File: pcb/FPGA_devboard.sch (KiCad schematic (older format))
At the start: 2 parts, among them X3 AC7020, X4 Conn_02x05_Odd_Even

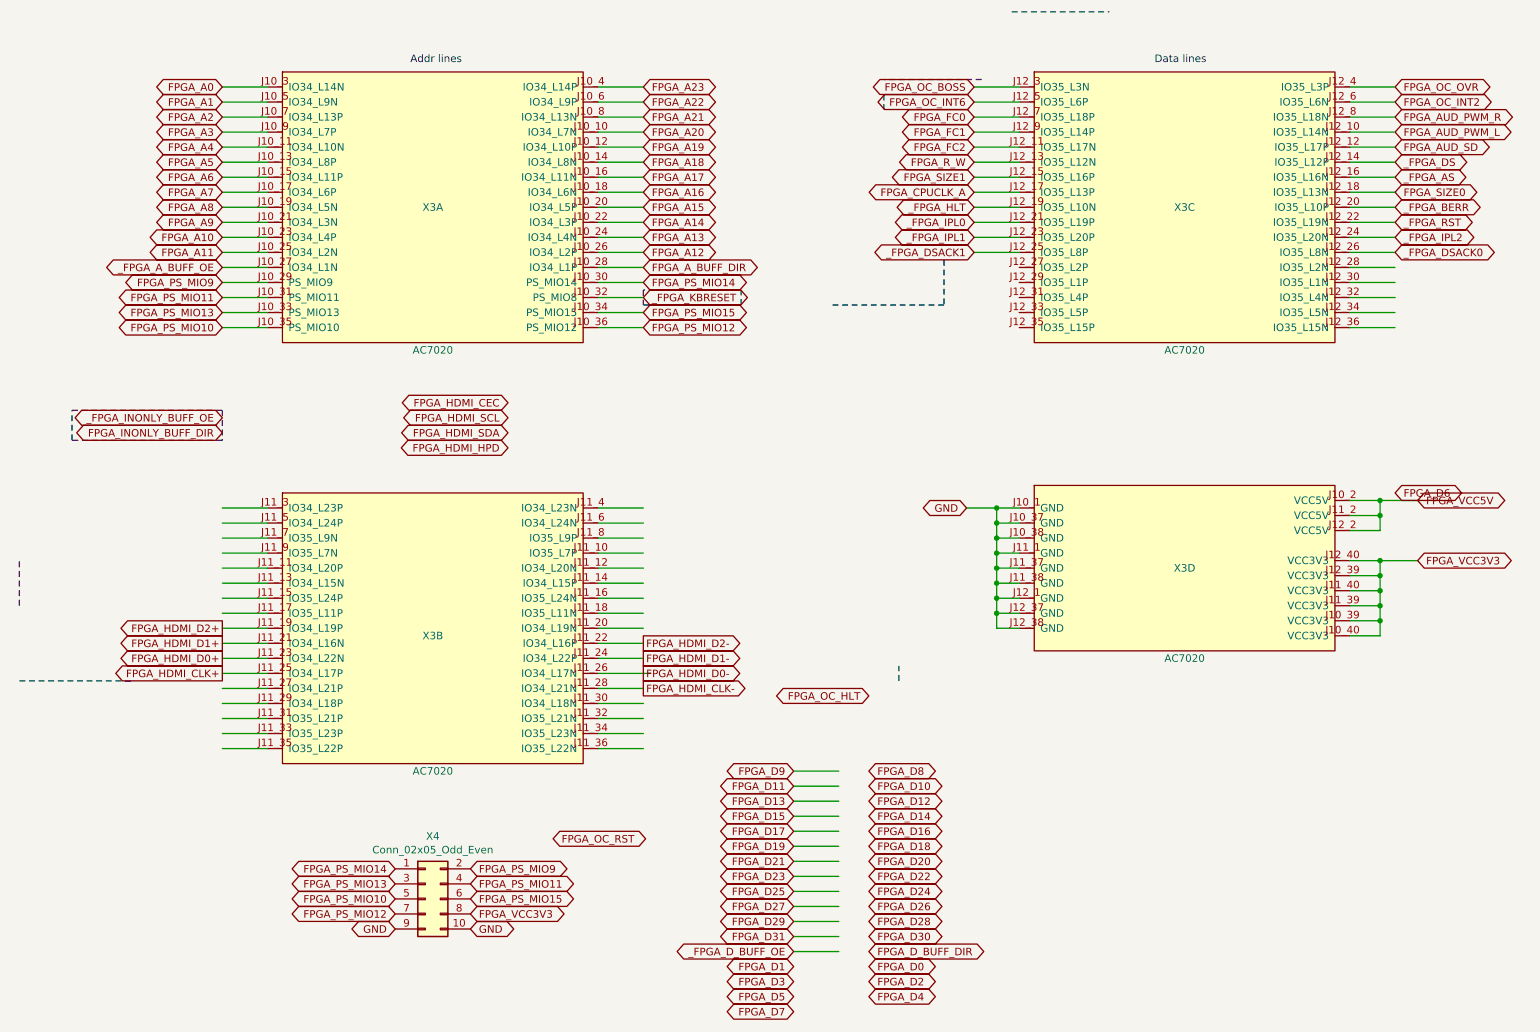
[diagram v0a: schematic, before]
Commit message: wire length aligns
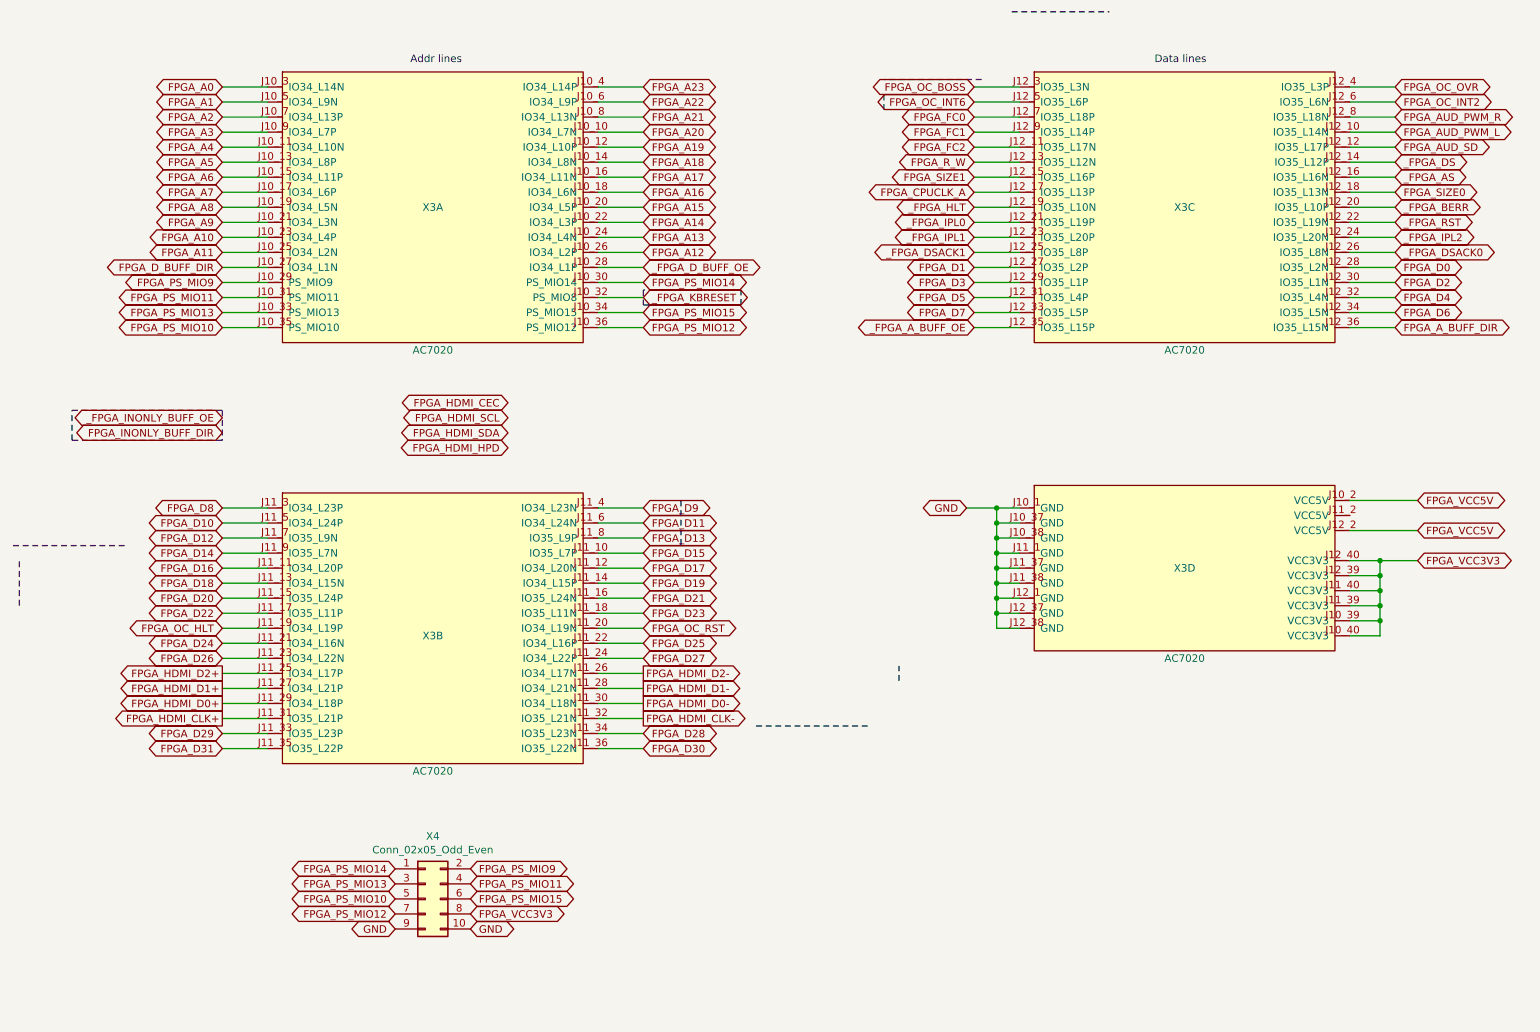
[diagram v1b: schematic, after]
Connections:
- wire segments 146 -> 134
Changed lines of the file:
@@
 	4300 6000 4600 6000
 Wire Wire Line
-	5600 7350 5900 7350
-Wire Wire Line
 	6800 1800 7100 1800
 Wire Wire Line
@@
 	6800 2100 7100 2100
 Wire Wire Line
-	5600 6150 5900 6150
-Wire Wire Line
-	5600 6250 5900 6250
-Wire Wire Line
-	5600 6350 5900 6350
-Wire Wire Line
-	5600 6450 5900 6450
-Wire Wire Line
-	5600 6550 5900 6550
-Wire Wire Line
-	5600 6650 5900 6650
-Wire Wire Line
-	5600 6750 5900 6750
-Wire Wire Line
-	5600 6850 5900 6850
-Wire Wire Line
-	5600 6950 5900 6950
-Wire Wire Line
-	5600 7050 5900 7050
-Wire Wire Line
-	5600 7150 5900 7150
-Wire Wire Line
-	5600 7250 5900 7250
+	6800 2800 7100 2800
+Wire Wire Line
+	6800 2900 7100 2900
+Wire Wire Line
+	6800 3000 7100 3000
+Wire Wire Line
+	6800 3100 7100 3100
+Wire Wire Line
+	6800 3200 7100 3200
 Wire Wire Line
 	9300 1600 9600 1600
@@
 Wire Wire Line
 	7100 5100 6950 5100
-Wire Wire Line
-	9300 4350 9500 4350
-Wire Wire Line
-	9300 4550 9500 4550
 Wire Wire Line
 	9300 4750 9500 4750
@@
 Text GLabel 9750 4350 2    50   BiDi ~ 0
 FPGA_VCC5V
-Wire Wire Line
-	9500 4350 9500 4450
-Connection ~ 9500 4350
-Wire Wire Line
-	9500 4350 9750 4350
-Connection ~ 9500 4450
-Wire Wire Line
-	9500 4450 9300 4450
-Wire Wire Line
-	9500 4450 9500 4550
 Wire Wire Line
 	9500 4750 9500 4850
@@
 Text GLabel 4600 1600 2    50   BiDi ~ 0
 FPGA_A23
+Text GLabel 9600 3200 2    50   BiDi ~ 0
+FPGA_A_BUFF_DIR
+Text GLabel 6800 3200 0    50   BiDi ~ 0
+_FPGA_A_BUFF_OE
+Text GLabel 9600 2800 2    50   BiDi ~ 0
+FPGA_D0
+Text GLabel 6800 2800 0    50   BiDi ~ 0
+FPGA_D1
+Text GLabel 9600 2900 2    50   BiDi ~ 0
+FPGA_D2
+Text GLabel 6800 2900 0    50   BiDi ~ 0
+FPGA_D3
+Text GLabel 9600 3000 2    50   BiDi ~ 0
+FPGA_D4
+Text GLabel 6800 3000 0    50   BiDi ~ 0
+FPGA_D5
+Text GLabel 9600 3100 2    50   BiDi ~ 0
+FPGA_D6
+Text GLabel 6800 3100 0    50   BiDi ~ 0
+FPGA_D7
+Text GLabel 1800 4400 0    50   BiDi ~ 0
+FPGA_D8
+Text GLabel 4600 4400 2    50   BiDi ~ 0
+FPGA_D9
+Text GLabel 1800 4500 0    50   BiDi ~ 0
+FPGA_D10
+Text GLabel 4600 4500 2    50   BiDi ~ 0
+FPGA_D11
+Text GLabel 1800 4600 0    50   BiDi ~ 0
+FPGA_D12
+Text GLabel 4600 4600 2    50   BiDi ~ 0
+FPGA_D13
+Text GLabel 1800 4700 0    50   BiDi ~ 0
+FPGA_D14
+Text GLabel 4600 4700 2    50   BiDi ~ 0
+FPGA_D15
+Text GLabel 1800 4800 0    50   BiDi ~ 0
+FPGA_D16
+Text GLabel 4600 4800 2    50   BiDi ~ 0
+FPGA_D17
+Text GLabel 1800 4900 0    50   BiDi ~ 0
+FPGA_D18
+Text GLabel 4600 4900 2    50   BiDi ~ 0
+FPGA_D19
+Text GLabel 1800 5000 0    50   BiDi ~ 0
+FPGA_D20
+Text GLabel 4600 5000 2    50   BiDi ~ 0
+FPGA_D21
+Text GLabel 1800 5100 0    50   BiDi ~ 0
+FPGA_D22
+Text GLabel 4600 5100 2    50   BiDi ~ 0
+FPGA_D23
+Text GLabel 1800 5300 0    50   BiDi ~ 0
+FPGA_D24
+Text GLabel 4600 5300 2    50   BiDi ~ 0
+FPGA_D25
+Text GLabel 1800 5400 0    50   BiDi ~ 0
+FPGA_D26
+Text GLabel 4600 5400 2    50   BiDi ~ 0
+FPGA_D27
+Text GLabel 4600 5900 2    50   BiDi ~ 0
+FPGA_D28
+Text GLabel 1800 5900 0    50   BiDi ~ 0
+FPGA_D29
+Text GLabel 4600 6000 2    50   BiDi ~ 0
+FPGA_D30
+Text GLabel 1800 6000 0    50   BiDi ~ 0
+FPGA_D31
+Text GLabel 1800 2800 0    50   BiDi ~ 0
+FPGA_D_BUFF_DIR
 Text GLabel 4600 2800 2    50   BiDi ~ 0
-FPGA_A_BUFF_DIR
-Text GLabel 1800 2800 0    50   BiDi ~ 0
-_FPGA_A_BUFF_OE
-Text GLabel 6100 7450 2    50   BiDi ~ 0
-FPGA_D0
-Text GLabel 5600 7450 0    50   BiDi ~ 0
-FPGA_D1
-Text GLabel 6100 7550 2    50   BiDi ~ 0
-FPGA_D2
-Text GLabel 5600 7550 0    50   BiDi ~ 0
-FPGA_D3
-Text GLabel 6100 7650 2    50   BiDi ~ 0
-FPGA_D4
-Text GLabel 5600 7650 0    50   BiDi ~ 0
-FPGA_D5
-Text GLabel 9600 4300 2    50   BiDi ~ 0
-FPGA_D6
-Text GLabel 5600 7750 0    50   BiDi ~ 0
-FPGA_D7
-Text GLabel 6100 6150 2    50   BiDi ~ 0
-FPGA_D8
-Text GLabel 5600 6150 0    50   BiDi ~ 0
-FPGA_D9
-Text GLabel 6100 6250 2    50   BiDi ~ 0
-FPGA_D10
-Text GLabel 5600 6250 0    50   BiDi ~ 0
-FPGA_D11
-Text GLabel 6100 6350 2    50   BiDi ~ 0
-FPGA_D12
-Text GLabel 5600 6350 0    50   BiDi ~ 0
-FPGA_D13
-Text GLabel 6100 6450 2    50   BiDi ~ 0
-FPGA_D14
-Text GLabel 5600 6450 0    50   BiDi ~ 0
-FPGA_D15
-Text GLabel 6100 6550 2    50   BiDi ~ 0
-FPGA_D16
-Text GLabel 5600 6550 0    50   BiDi ~ 0
-FPGA_D17
-Text GLabel 6100 6650 2    50   BiDi ~ 0
-FPGA_D18
-Text GLabel 5600 6650 0    50   BiDi ~ 0
-FPGA_D19
-Text GLabel 6100 6750 2    50   BiDi ~ 0
-FPGA_D20
-Text GLabel 5600 6750 0    50   BiDi ~ 0
-FPGA_D21
-Text GLabel 6100 6850 2    50   BiDi ~ 0
-FPGA_D22
-Text GLabel 5600 6850 0    50   BiDi ~ 0
-FPGA_D23
-Text GLabel 6100 6950 2    50   BiDi ~ 0
-FPGA_D24
-Text GLabel 5600 6950 0    50   BiDi ~ 0
-FPGA_D25
-Text GLabel 6100 7050 2    50   BiDi ~ 0
-FPGA_D26
-Text GLabel 5600 7050 0    50   BiDi ~ 0
-FPGA_D27
-Text GLabel 6100 7150 2    50   BiDi ~ 0
-FPGA_D28
-Text GLabel 5600 7150 0    50   BiDi ~ 0
-FPGA_D29
-Text GLabel 6100 7250 2    50   BiDi ~ 0
-FPGA_D30
-Text GLabel 5600 7250 0    50   BiDi ~ 0
-FPGA_D31
-Text GLabel 6100 7350 2    50   BiDi ~ 0
-FPGA_D_BUFF_DIR
-Text GLabel 5600 7350 0    50   BiDi ~ 0
 _FPGA_D_BUFF_OE
-Text GLabel 9600 1900 2    50   BiDi ~ 0
-FPGA_AUD_PWM_L
-Text GLabel 9600 1800 2    50   BiDi ~ 0
-FPGA_AUD_PWM_R
-Text GLabel 9600 2000 2    50   BiDi ~ 0
-FPGA_AUD_SD
-Text GLabel 4000 6600 2    50   BiDi ~ 0
+Text GLabel 4600 5200 2    50   BiDi ~ 0
 FPGA_OC_RST
 Text GLabel 2950 7200 0    50   BiDi ~ 0
@@
 	450  5050 450  4750
 Wire Notes Line
-	450  5550 1200 5550
-Wire Notes Line
-	6600 3050 5850 3050
+	5350 5850 6100 5850
+Wire Notes Line
+	1150 4650 400  4650
 Wire Notes Line
 	6200 1650 6200 1750
@@
 Wire Notes Line
 	4600 3050 5250 3050
-Text GLabel 1800 5200 0    50   Output ~ 0
+Text GLabel 1800 5500 0    50   Output ~ 0
 FPGA_HDMI_D2+
-Text GLabel 4600 5300 2    50   Output ~ 0
+Text GLabel 4600 5500 2    50   Output ~ 0
 FPGA_HDMI_D2-
-Text GLabel 1800 5300 0    50   Output ~ 0
+Text GLabel 1800 5600 0    50   Output ~ 0
 FPGA_HDMI_D1+
-Text GLabel 1800 5400 0    50   Output ~ 0
+Text GLabel 1800 5700 0    50   Output ~ 0
 FPGA_HDMI_D0+
-Text GLabel 4600 5500 2    50   Output ~ 0
+Text GLabel 4600 5700 2    50   Output ~ 0
 FPGA_HDMI_D0-
-Text GLabel 4600 5400 2    50   Output ~ 0
+Text GLabel 4600 5600 2    50   Output ~ 0
 FPGA_HDMI_D1-
-Text GLabel 1800 5500 0    50   Output ~ 0
+Text GLabel 1800 5800 0    50   Output ~ 0
 FPGA_HDMI_CLK+
 Wire Notes Line
@@
 Wire Notes Line
 	800  3750 1800 3750
-Text GLabel 9600 2200 2    50   BiDi ~ 0
-_FPGA_AS
-Text GLabel 6800 2200 0    50   BiDi ~ 0
-FPGA_SIZE1
-Text GLabel 9600 2300 2    50   BiDi ~ 0
-FPGA_SIZE0
 Text GLabel 1800 3900 0    50   BiDi ~ 0
 FPGA_INONLY_BUFF_DIR
@@
 _FPGA_INONLY_BUFF_OE
 Wire Notes Line
-	6600 2750 6600 3050
-Text GLabel 4600 5600 2    50   Output ~ 0
+	4850 4350 4850 4650
+Text GLabel 4600 5800 2    50   Output ~ 0
 FPGA_HDMI_CLK-
 Wire Wire Line
@@
 FPGA_HDMI_HPD
 Wire Wire Line
-	4300 5500 4650 5500
+	4300 5500 4600 5500
 Text GLabel 3450 6800 2    50   BiDi ~ 0
 FPGA_PS_MIO9
@@
 Wire Notes Line
 	6850 1550 6200 1550
-Text GLabel 6800 2600 0    50   BiDi ~ 0
-_FPGA_IPL1
-Text GLabel 6800 2500 0    50   BiDi ~ 0
-_FPGA_IPL0
-Text GLabel 6800 2400 0    50   BiDi ~ 0
-_FPGA_HLT
-Text GLabel 6800 2700 0    50   BiDi ~ 0
-_FPGA_DSACK1
 Text GLabel 9600 1600 2    50   BiDi ~ 0
 FPGA_OC_OVR
 Text GLabel 6800 1700 0    50   BiDi ~ 0
 FPGA_OC_INT6
-Text GLabel 6100 5650 0    50   BiDi ~ 0
+Text GLabel 1800 5200 0    50   BiDi ~ 0
 FPGA_OC_HLT
 Text GLabel 6800 1600 0    50   BiDi ~ 0
 FPGA_OC_BOSS
+Wire Wire Line
+	6800 2200 7100 2200
+Wire Wire Line
+	7100 2300 6800 2300
+Wire Wire Line
+	6800 2400 7100 2400
+Wire Wire Line
+	7100 2500 6800 2500
+Wire Wire Line
+	6800 2600 7100 2600
+Wire Wire Line
+	7100 1600 6800 1600
+Wire Wire Line
+	6800 1700 7100 1700
+Wire Wire Line
+	7100 2700 6800 2700
+Text GLabel 9750 4550 2    50   BiDi ~ 0
+FPGA_VCC5V
+Wire Wire Line
+	9300 4350 9750 4350
+Wire Wire Line
+	9300 4550 9750 4550
+Text GLabel 9600 2100 2    50   BiDi ~ 0
+_FPGA_DS
+Text GLabel 9600 2300 2    50   BiDi ~ 0
+FPGA_SIZE0
+Text GLabel 9600 2200 2    50   BiDi ~ 0
+_FPGA_AS
+Text GLabel 9600 2000 2    50   BiDi ~ 0
+FPGA_AUD_SD
+Text GLabel 9600 1800 2    50   BiDi ~ 0
+FPGA_AUD_PWM_R
+Text GLabel 9600 1900 2    50   BiDi ~ 0
+FPGA_AUD_PWM_L
+Text GLabel 6800 2000 0    50   BiDi ~ 0
+FPGA_FC2
+Text GLabel 6800 1900 0    50   BiDi ~ 0
+FPGA_FC1
+Text GLabel 6800 1800 0    50   BiDi ~ 0
+FPGA_FC0
 Text GLabel 6800 2100 0    50   BiDi ~ 0
 FPGA_R_W
-Text GLabel 6800 1800 0    50   BiDi ~ 0
-FPGA_FC0
-Text GLabel 6800 1900 0    50   BiDi ~ 0
-FPGA_FC1
-Text GLabel 6800 2000 0    50   BiDi ~ 0
-FPGA_FC2
-Text GLabel 9600 2100 2    50   BiDi ~ 0
-_FPGA_DS
-Wire Wire Line
-	6800 2200 7100 2200
-Wire Wire Line
-	7100 2300 6800 2300
-Wire Wire Line
-	6800 2400 7100 2400
-Wire Wire Line
-	7100 2500 6800 2500
-Wire Wire Line
-	6800 2600 7100 2600
-Wire Wire Line
-	7100 1600 6800 1600
-Wire Wire Line
-	6800 1700 7100 1700
-Wire Wire Line
-	7100 2700 6800 2700
+Text GLabel 6800 2200 0    50   BiDi ~ 0
+FPGA_SIZE1
+Text GLabel 6800 2300 0    50   BiDi ~ 0
+FPGA_CPUCLK_A
+Text GLabel 6800 2700 0    50   BiDi ~ 0
+_FPGA_DSACK1
+Text GLabel 6800 2400 0    50   BiDi ~ 0
+_FPGA_HLT
+Text GLabel 6800 2500 0    50   BiDi ~ 0
+_FPGA_IPL0
+Text GLabel 6800 2600 0    50   BiDi ~ 0
+_FPGA_IPL1
+Text GLabel 9600 2400 2    50   BiDi ~ 0
+_FPGA_BERR
+Text GLabel 9600 2500 2    50   BiDi ~ 0
+_FPGA_RST
+Text GLabel 9600 2600 2    50   BiDi ~ 0
+_FPGA_IPL2
 Text GLabel 9600 2700 2    50   BiDi ~ 0
 _FPGA_DSACK0
-Text GLabel 9600 2600 2    50   BiDi ~ 0
-_FPGA_IPL2
-Text GLabel 9600 2500 2    50   BiDi ~ 0
-_FPGA_RST
-Text GLabel 9600 2400 2    50   BiDi ~ 0
-_FPGA_BERR
-Text GLabel 6800 2300 0    50   BiDi ~ 0
-FPGA_CPUCLK_A
 $EndSCHEMATC

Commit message: Some more work done
I'm too lazy to think about commit messages in my pet project, really
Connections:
- net FPGA_VCC5V renamed FPGA_VCC5V_1
- net FPGA_VCC5V_1: no longer X3.J12_2 (VCC5V)
- new net FPGA_VCC5V_2: X3.J12_2 (VCC5V)
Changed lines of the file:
@@
 	6950 5200 7100 5200
 Text GLabel 9750 4350 2    50   BiDi ~ 0
-FPGA_VCC5V
+FPGA_VCC5V_1
 Wire Wire Line
 	9500 4750 9500 4850
@@
 	7100 2700 6800 2700
 Text GLabel 9750 4550 2    50   BiDi ~ 0
-FPGA_VCC5V
+FPGA_VCC5V_2
 Wire Wire Line
 	9300 4350 9750 4350

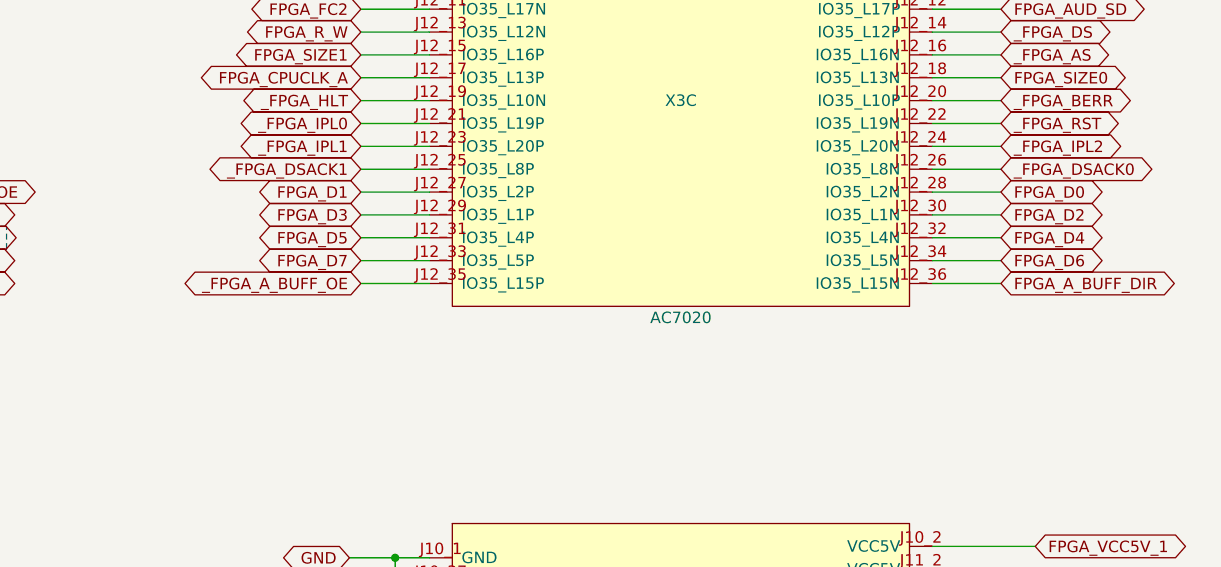
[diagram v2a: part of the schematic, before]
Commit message: bigger vias, fixing DRC issues
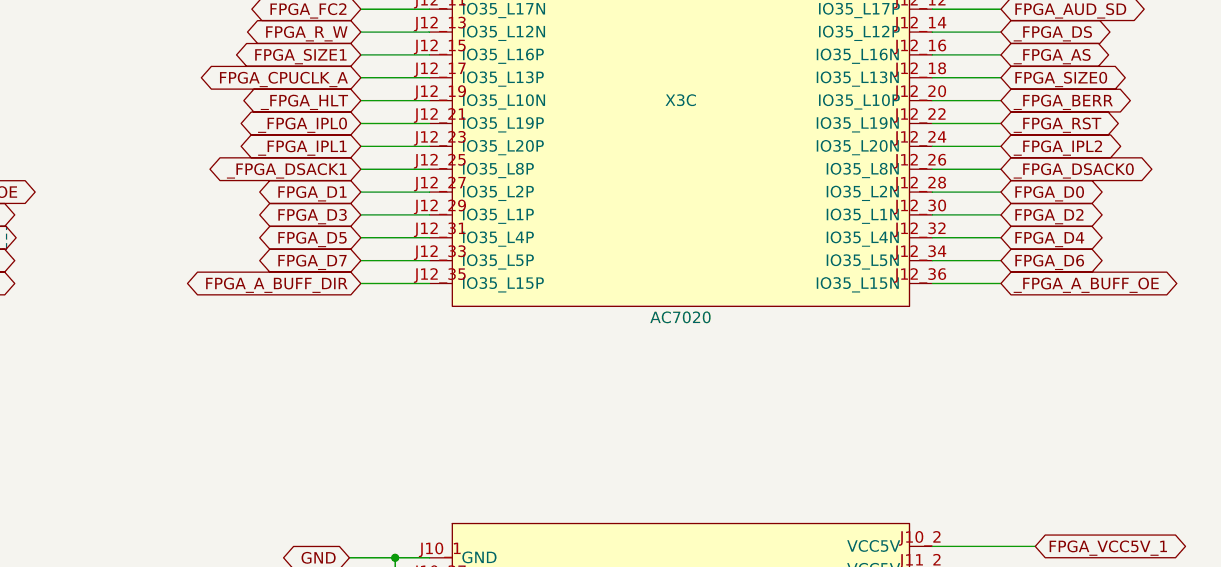
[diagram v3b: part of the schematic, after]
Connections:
- net FPGA_A_BUFF_DIR: now also X3.J12_35 (IO35_L15P); no longer X3.J12_36 (IO35_L15N)
- net _FPGA_A_BUFF_OE: now also X3.J12_36 (IO35_L15N); no longer X3.J12_35 (IO35_L15P)
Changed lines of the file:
@@
 Text GLabel 4600 1600 2    50   BiDi ~ 0
 FPGA_A23
+Text GLabel 6800 3200 0    50   BiDi ~ 0
+FPGA_A_BUFF_DIR
 Text GLabel 9600 3200 2    50   BiDi ~ 0
-FPGA_A_BUFF_DIR
-Text GLabel 6800 3200 0    50   BiDi ~ 0
 _FPGA_A_BUFF_OE
 Text GLabel 9600 2800 2    50   BiDi ~ 0

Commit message: ready for production
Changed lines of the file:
@@
 $Descr A4 11693 8268
 encoding utf-8
-Sheet 10 11
+Sheet 9 10
 Title "Wishmaster 1200"
-Date ""
+Date "2020-03-16"
 Rev "ES1"
 Comp "Created by Konfusion in 2020"
@@
 	4600 3200 4300 3200
 Wire Notes Line
-	450  5050 450  4750
-Wire Notes Line
-	5350 5850 6100 5850
-Wire Notes Line
-	1150 4650 400  4650
-Wire Notes Line
-	6200 1650 6200 1750
-Wire Notes Line
 	1800 3750 1800 3950
 Wire Notes Line
@@
 Text GLabel 1800 3800 0    50   BiDi ~ 0
 _FPGA_INONLY_BUFF_OE
-Wire Notes Line
-	4850 4350 4850 4650
 Text GLabel 4600 5800 2    50   Output ~ 0
 FPGA_HDMI_CLK-
@@
 Text GLabel 9600 1700 2    50   BiDi ~ 0
 FPGA_OC_INT2
-Wire Notes Line
-	6300 5550 6300 5450
-Wire Notes Line
-	7050 1100 7700 1100
-Wire Notes Line
-	6850 1550 6200 1550
 Text GLabel 9600 1600 2    50   BiDi ~ 0
 FPGA_OC_OVR

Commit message: board updated - factory DRC checking in progress
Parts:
- X4: footprint Connector_PinHeader_2.54mm:PinHeader_2x05_P2.54mm_Vertical -> WM1200:PinHeader_2x05_P2.54mm_Vertical
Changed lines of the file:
@@
 F 0 "X4" H 3200 7417 50  0000 C CNN
 F 1 "Conn_02x05_Odd_Even" H 3200 7326 50  0000 C CNN
-F 2 "Connector_PinHeader_2.54mm:PinHeader_2x05_P2.54mm_Vertical" H 3150 7000 50  0001 C CNN
+F 2 "WM1200:PinHeader_2x05_P2.54mm_Vertical" H 3150 7000 50  0001 C CNN
 F 3 "~" H 3150 7000 50  0001 C CNN
 	1    3150 7000
